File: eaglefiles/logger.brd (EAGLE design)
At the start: 43.2 x 20 mm, 35 parts, among them K1 65100516121, Q2 IRLML9301, U1 MCP1640, U3 FT232RLSSOP

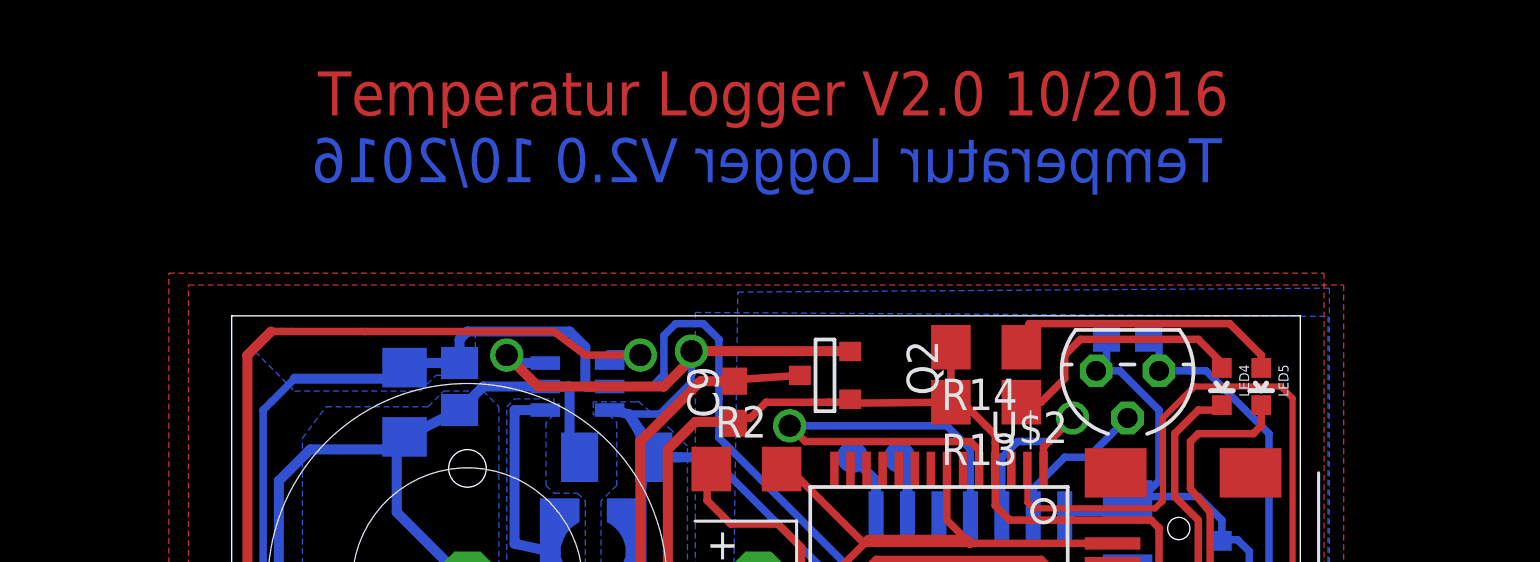
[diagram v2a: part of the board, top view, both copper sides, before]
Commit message: Corrected direction of mosfet & copied lib for tsic
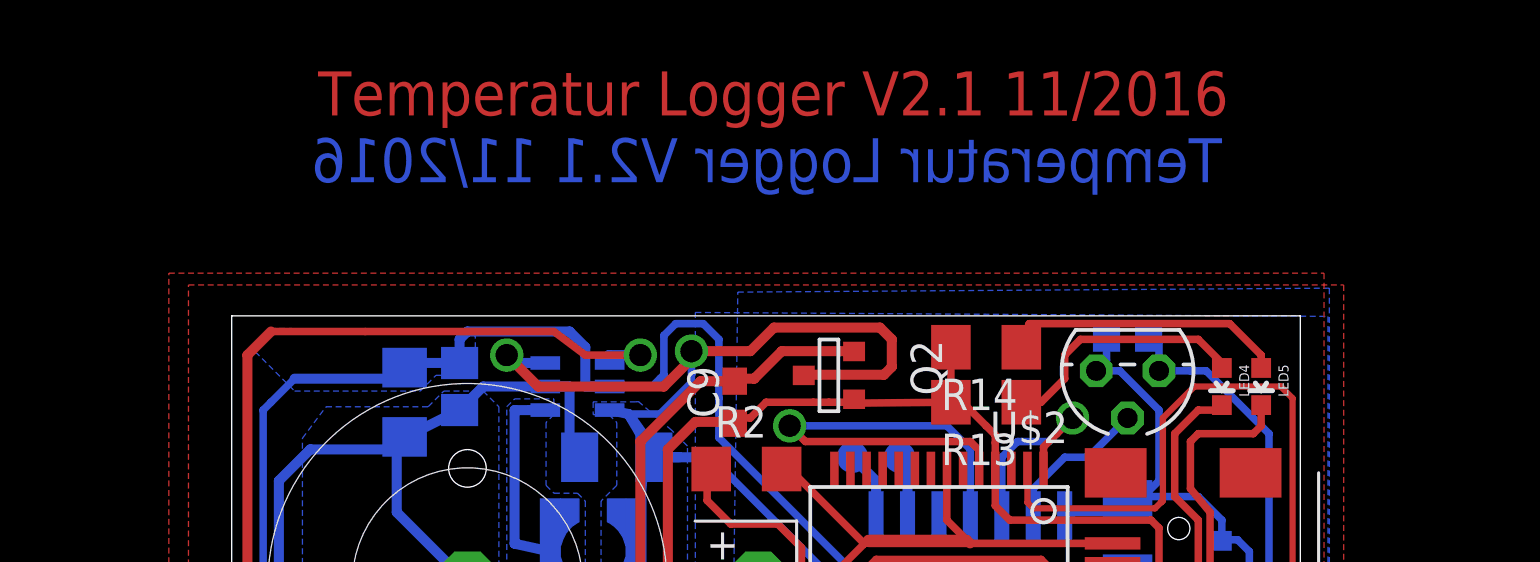
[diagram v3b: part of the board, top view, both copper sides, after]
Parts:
- R13, R14: value 1K -> 1k8
- R3: value 1,8k -> 1k8
- R5: value (none) -> 680k
- R6: value (none) -> 220k
- moved Q2 0.16 mm to (24.1, 17.6)
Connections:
- net N$6: now also Q2.2; no longer Q2.1
- net VSUPPLY: now also Q2.1; no longer Q2.2
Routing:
- net VSUPPLY: track 47.0 -> 54.1 mm
- net N$6: track 28.4 -> 31.0 mm
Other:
- board text added: "Temperatur Logger V2.1 11/2016"
- board text removed: "Temperatur Logger V2.0 10/2016"
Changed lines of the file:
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@@
 <wire x1="43.175" y1="0" x2="43.175" y2="20" width="0" layer="20"/>
 <wire x1="43.175" y1="20" x2="0" y2="20" width="0" layer="20"/>
-<text x="40.005" y="25.4" size="1.778" layer="16" rot="MR0">Temperatur Logger V2.0 10/2016</text>
+<text x="40.005" y="25.4" size="1.778" layer="16" rot="MR0">Temperatur Logger V2.1 11/2016</text>
 <wire x1="0" y1="0" x2="0" y2="20" width="0" layer="20"/>
 <circle x="38.265" y="7.008" radius="0.35" width="0.3" layer="116"/>
@@
 <circle x="11.113" y="18.415" radius="0.35" width="0.3" layer="116"/>
 <circle x="18.574" y="18.574" radius="0.35" width="0.3" layer="116"/>
-<text x="3.4925" y="28.09875" size="1.778" layer="1">Temperatur Logger V2.0 10/2016</text>
+<text x="3.4925" y="28.09875" size="1.778" layer="1">Temperatur Logger V2.1 11/2016</text>
 <circle x="22.8605" y="1.429" radius="0.35" width="0.3" layer="116"/>
 </plain>
@@
 <element name="C2" library="rcl" package="C1206K" value="100nF" x="36.195" y="11.1125" rot="MR90"/>
 <element name="LED3" library="led" package="CHIPLED_0603" value="lc green" x="40.005" y="10.16" rot="MR0"/>
-<element name="R3" library="eagle-ltspice" package="R1206" value="1,8k" x="36.83" y="4.1275" rot="MR0">
+<element name="R3" library="eagle-ltspice" package="R1206" value="1k8" x="36.83" y="4.1275" rot="MR0">
 <attribute name="SPICEMODEL" value="NONE" x="36.83" y="-2.2225" size="1.778" layer="28" rot="MR0" display="off"/>
 <attribute name="SPICEPREFIX" value="R" x="36.83" y="-2.2225" size="1.778" layer="28" rot="MR0" display="off"/>
@@
 <element name="U1" library="karlnet-parts" package="SOT23-6" value="MCP1640" x="13.97" y="17.145" rot="MR90"/>
 <element name="C3" library="rcl" package="C1206K" value="4,7uF" x="15.5575" y="14.2875" rot="MR0"/>
-<element name="R5" library="resistor" package="R1206" value="" x="6.985" y="2.8575" rot="MR0"/>
-<element name="R6" library="resistor" package="R1206" value="" x="12.7" y="2.8575" rot="MR0"/>
+<element name="R5" library="resistor" package="R1206" value="680k" x="6.985" y="2.8575" rot="MR0"/>
+<element name="R6" library="resistor" package="R1206" value="220k" x="12.7" y="2.8575" rot="MR0"/>
 <element name="L1" library="EagleLibrary_Wuerth_Elektronik_eiSos_rev16a" package="WE-TPC_3816" value="4,7uH" x="14.605" y="10.4775" rot="MR0"/>
 <element name="C4" library="resistor" package="C0805" value="680nF" x="9.2075" y="17.145" rot="MR270"/>
@@
 <element name="C5" library="rcl" package="C0603" value="100nF" x="36.195" y="19.05" rot="MR0"/>
 <element name="U3" library="SparkFun" package="SSOP28DB" value="FT232RLSSOP" x="28.575" y="10.16" rot="R180"/>
-<element name="R13" library="rcl" package="R1206" value="1K" x="30.48" y="16.51" rot="R180"/>
-<element name="R14" library="rcl" package="R1206" value="1K" x="30.48" y="18.7325" rot="R180"/>
+<element name="R13" library="rcl" package="R1206" value="1k8" x="30.48" y="16.51" rot="R180"/>
+<element name="R14" library="rcl" package="R1206" value="1k8" x="30.48" y="18.7325" rot="R180"/>
 <element name="LED4" library="SparkFun" package="LED-0603" value="Red" x="40.005" y="17.145" rot="R180"/>
 <element name="LED5" library="SparkFun" package="LED-0603" value="Green" x="41.5925" y="17.145" rot="R180"/>
 <element name="C7" library="rcl" package="C1206" value="100nF" x="33.02" y="3.175" rot="R270"/>
 <element name="C8" library="rcl" package="C0603" value="100nF" x="25.7175" y="4.445"/>
-<element name="Q2" library="0liver" package="SOT-23" value="IRLML9301" x="23.97125" y="17.62125" rot="R270"/>
+<element name="Q2" library="0liver" package="SOT-23" value="IRLML9301" x="24.13" y="17.62125" rot="R270"/>
 <element name="R2" library="eagle-ltspice" package="R1206" value="100k" x="20.79625" y="13.81125">
 <attribute name="SPICEPREFIX" value="R" x="20.79625" y="13.81125" size="1.778" layer="27" display="off"/>
@@
 <vertex x="16.3275" y="16.5259375"/>
 </polygon>
-<contactref element="Q2" pad="2"/>
 <wire x1="18.0975" y1="14.2875" x2="19.3675" y2="14.2875" width="0.3048" layer="16"/>
 <wire x1="19.3675" y1="14.2875" x2="25.0825" y2="8.5725" width="0.3048" layer="16"/>
@@
 <wire x1="16.8275" y1="14.9225" x2="16.03375" y2="16.03375" width="0.4064" layer="16"/>
 <via x="18.57375" y="18.57375" extent="1-16" drill="0.9" shape="octagon"/>
-<wire x1="18.57375" y1="18.57375" x2="24.97455" y2="18.57375" width="0.4064" layer="1"/>
-<wire x1="24.97455" y1="18.57375" x2="24.98725" y2="18.56105" width="0.4064" layer="1" curve="-90"/>
 <wire x1="11.1125" y1="18.415" x2="12.3825" y2="17.145" width="0.4064" layer="1"/>
 <wire x1="12.3825" y1="17.145" x2="17.4625" y2="17.145" width="0.4064" layer="1"/>
@@
 <wire x1="17.30375" y1="16.03375" x2="18.57375" y2="17.30375" width="0.3048" layer="16"/>
 <wire x1="18.57375" y1="17.30375" x2="18.57375" y2="18.57375" width="0.3048" layer="16"/>
+<contactref element="Q2" pad="1"/>
+<wire x1="18.57375" y1="18.57375" x2="20.955" y2="18.57375" width="0.4064" layer="1"/>
+<wire x1="20.955" y1="18.57375" x2="21.9075" y2="19.52625" width="0.4064" layer="1"/>
+<wire x1="21.9075" y1="19.52625" x2="26.19375" y2="19.52625" width="0.4064" layer="1"/>
+<wire x1="26.19375" y1="19.52625" x2="26.67" y2="19.05" width="0.4064" layer="1"/>
+<wire x1="26.67" y1="19.05" x2="26.67" y2="17.93875" width="0.4064" layer="1"/>
+<wire x1="26.67" y1="17.93875" x2="26.3525" y2="17.62125" width="0.4064" layer="1"/>
+<wire x1="26.3525" y1="17.62125" x2="23.1394" y2="17.62125" width="0.4064" layer="1"/>
+<wire x1="23.1394" y1="17.62125" x2="23.114" y2="17.59585" width="0.4064" layer="1"/>
 </signal>
 <signal name="N$32">
@@
 <wire x1="36.83" y1="7.62" x2="37.465" y2="8.255" width="0.3048" layer="1"/>
 <wire x1="37.465" y1="8.255" x2="37.465" y2="11.43" width="0.3048" layer="1"/>
-<wire x1="24.98725" y1="16.63065" x2="24.8924" y2="16.4719" width="0.3048" layer="1"/>
+<wire x1="25.146" y1="16.63065" x2="24.8924" y2="16.4719" width="0.3048" layer="1"/>
 <wire x1="24.8924" y1="16.4719" x2="29.058" y2="16.51" width="0.3048" layer="1"/>
 <wire x1="29.058" y1="16.51" x2="29.5275" y2="16.51" width="0.3048" layer="1"/>
@@
 <wire x1="30.85" y1="13.816" x2="30.85" y2="14.87" width="0.3048" layer="1"/>
 <wire x1="29.058" y1="18.7325" x2="29.058" y2="16.51" width="0.3048" layer="1"/>
-<wire x1="24.98725" y1="16.63065" x2="24.88565" y2="16.63065" width="0.3048" layer="1"/>
+<wire x1="25.146" y1="16.63065" x2="24.88565" y2="16.63065" width="0.3048" layer="1"/>
 <wire x1="24.88565" y1="16.63065" x2="24.92375" y2="16.51" width="0.3048" layer="1"/>
 <wire x1="24.92375" y1="16.51" x2="24.13" y2="16.51" width="0.3048" layer="1"/>
@@
 <signal name="N$6">
 <contactref element="U$1" pad="P$2"/>
-<contactref element="Q2" pad="1"/>
 <contactref element="C9" pad="2"/>
-<wire x1="22.95525" y1="17.59585" x2="20.6121" y2="17.4371" width="0.3048" layer="1"/>
 <wire x1="20.6121" y1="17.4371" x2="20.6375" y2="17.4625" width="0.3048" layer="1"/>
 <wire x1="20.6375" y1="17.4625" x2="20.4225" y2="17.4625" width="0.3048" layer="1"/>
@@
 <wire x1="20.955" y1="3.96875" x2="20.955" y2="9.36375" width="0.4064" layer="1"/>
 <wire x1="20.955" y1="9.36375" x2="21.275" y2="9.2075" width="0.4064" layer="1"/>
+<contactref element="Q2" pad="2"/>
+<wire x1="20.6375" y1="17.4625" x2="21.11375" y2="17.4625" width="0.4064" layer="1"/>
+<wire x1="21.11375" y1="17.4625" x2="22.225" y2="18.57375" width="0.4064" layer="1"/>
+<wire x1="22.225" y1="18.57375" x2="25.1333" y2="18.57375" width="0.4064" layer="1"/>
+<wire x1="25.1333" y1="18.57375" x2="25.146" y2="18.56105" width="0.4064" layer="1"/>
 </signal>
 <signal name="5V">

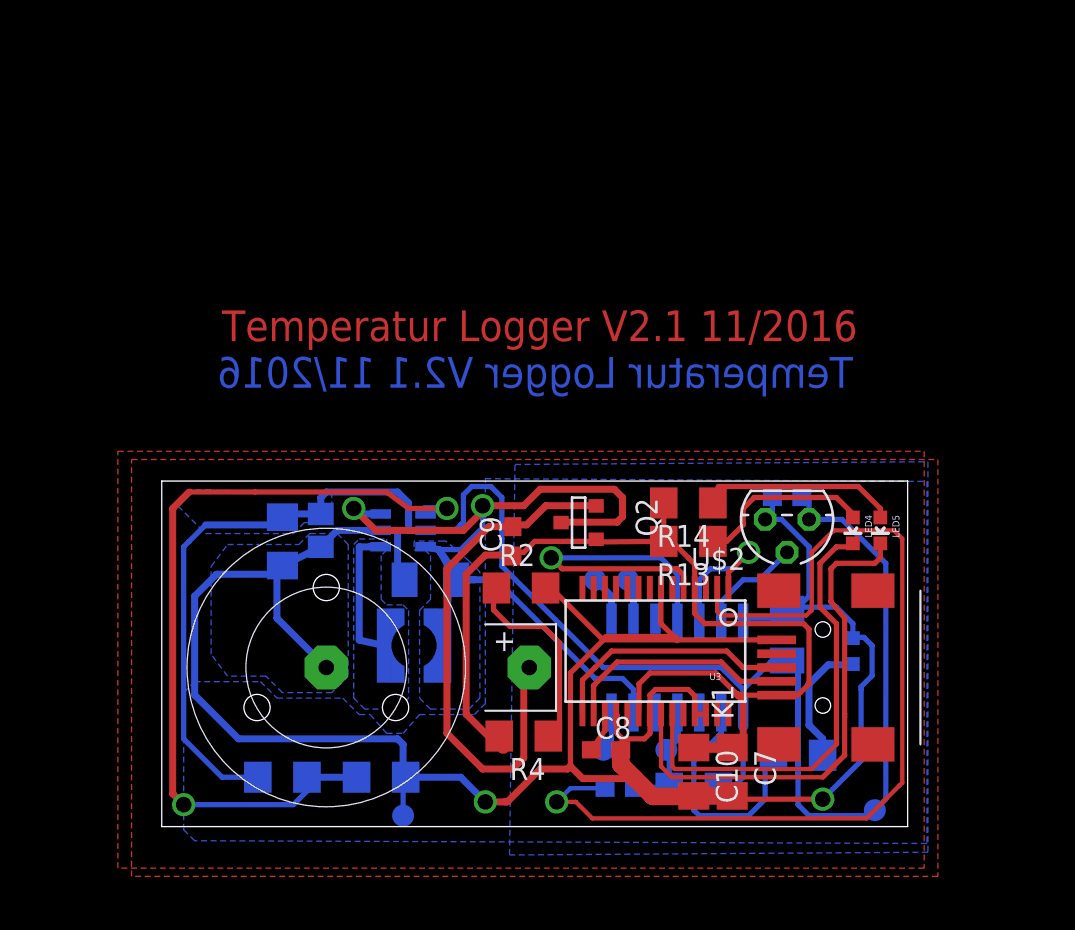
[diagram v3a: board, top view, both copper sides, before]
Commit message: Added diode for 5V usb port
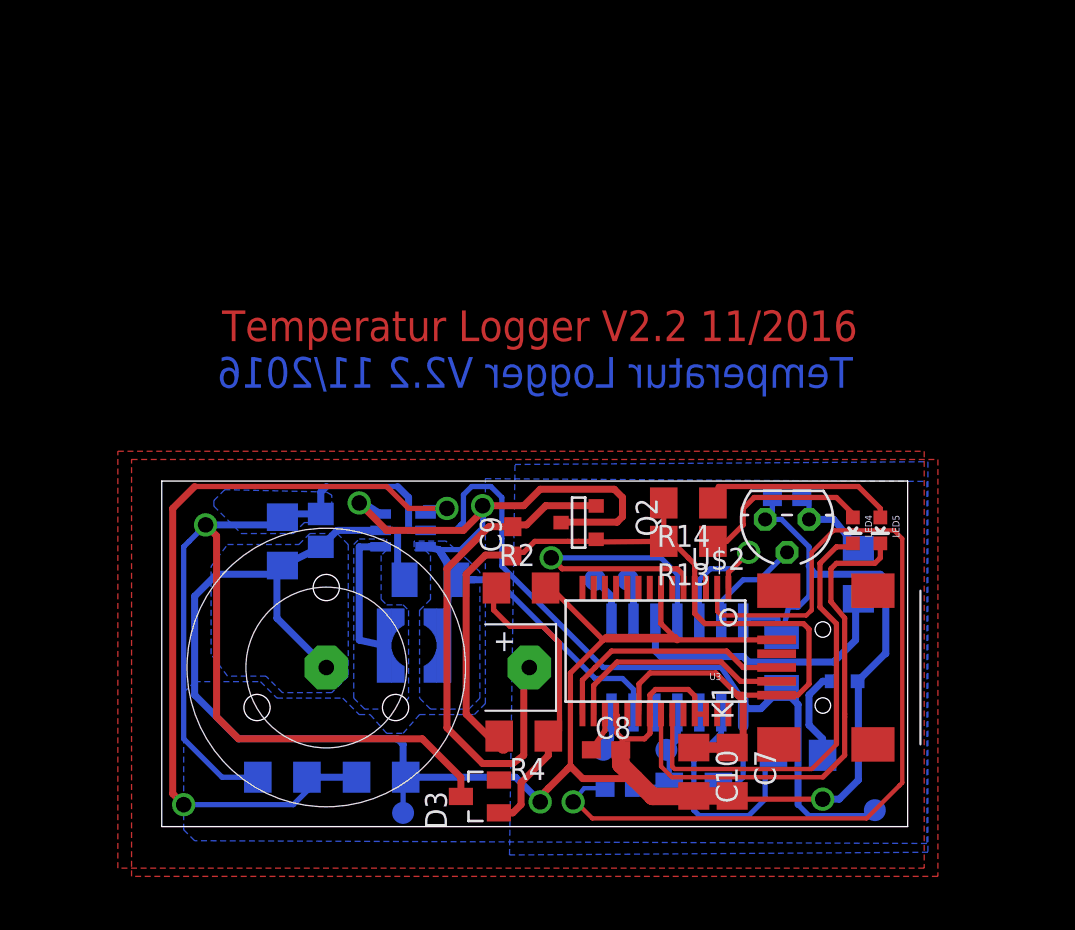
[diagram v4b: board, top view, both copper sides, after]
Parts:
- added D3: PMEG2010AET, diode:SOT23
- added R7: 220, resistor:R1206
- moved LED3 1.81 mm to (39.5, 8.41), turned to 90 degrees
- moved C2 1.62 mm to (35.9, 9.53)
- moved U$10 0.16 mm to (14.0, 0.79)
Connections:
- new net N$10: C5.1, R7.2, U$2.1
- new net N$9: IC1.10, R7.1
- net 5V: now also D3.1
- net VCC: now also D3.3; no longer C5.1, U$2.1
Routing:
- net N$9: track 0.00 -> 16.6 mm
- net 5V: track 11.7 -> 17.8 mm
- net GND: track 146.3 -> 152.1 mm
- net N$10: track 0.00 -> 5.29 mm
- net N$19: track 7.47 -> 5.60 mm
- net N$8: track 55.0 -> 53.1 mm
- net VCC: track 114.0 -> 112.5 mm, vias 0 -> 1
- net N$6: track 31.0 -> 30.4 mm
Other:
- board text added: "Temperatur Logger V2.2 11/2016"
- board text removed: "Temperatur Logger V2.1 11/2016"

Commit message: Added option to trigger 5V supply voltage only on demand
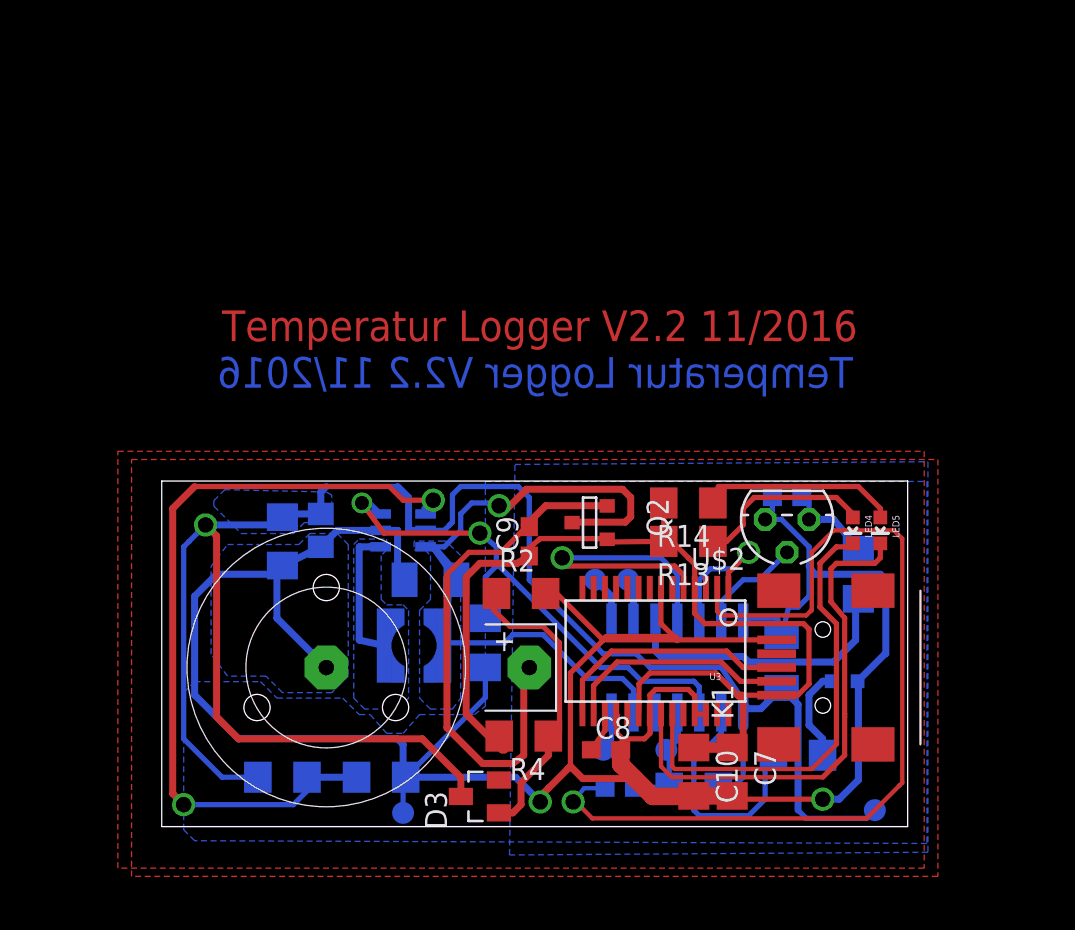
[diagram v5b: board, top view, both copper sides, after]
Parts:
- added R8: 68k, resistor:R1206
- moved C9 0.95 mm to (21.3, 16.5)
- moved Q2 0.64 mm to (24.8, 17.6)
- moved R2 0.32 mm to (20.8, 13.5)
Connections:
- new net ENABLE: IC1.3, R8.2, U1.3
- net GND: now also R8.1
- net VSUPPLY: no longer U1.3
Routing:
- net ENABLE: track 0.00 -> 31.2 mm, vias 0 -> 2
- net VSUPPLY: track 54.5 -> 42.4 mm, vias 2 -> 1
- net GND: track 152.1 -> 160.5 mm
- net N$5: track 48.4 -> 46.8 mm
- net N$1: track 19.3 -> 18.1 mm
- net N$6: track 30.4 -> 31.6 mm
- net VCC: track 112.5 -> 113.3 mm
